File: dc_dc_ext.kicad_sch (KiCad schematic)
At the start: 30 parts, among them U10 TPS56339DDC, U11 TPS56339DDC

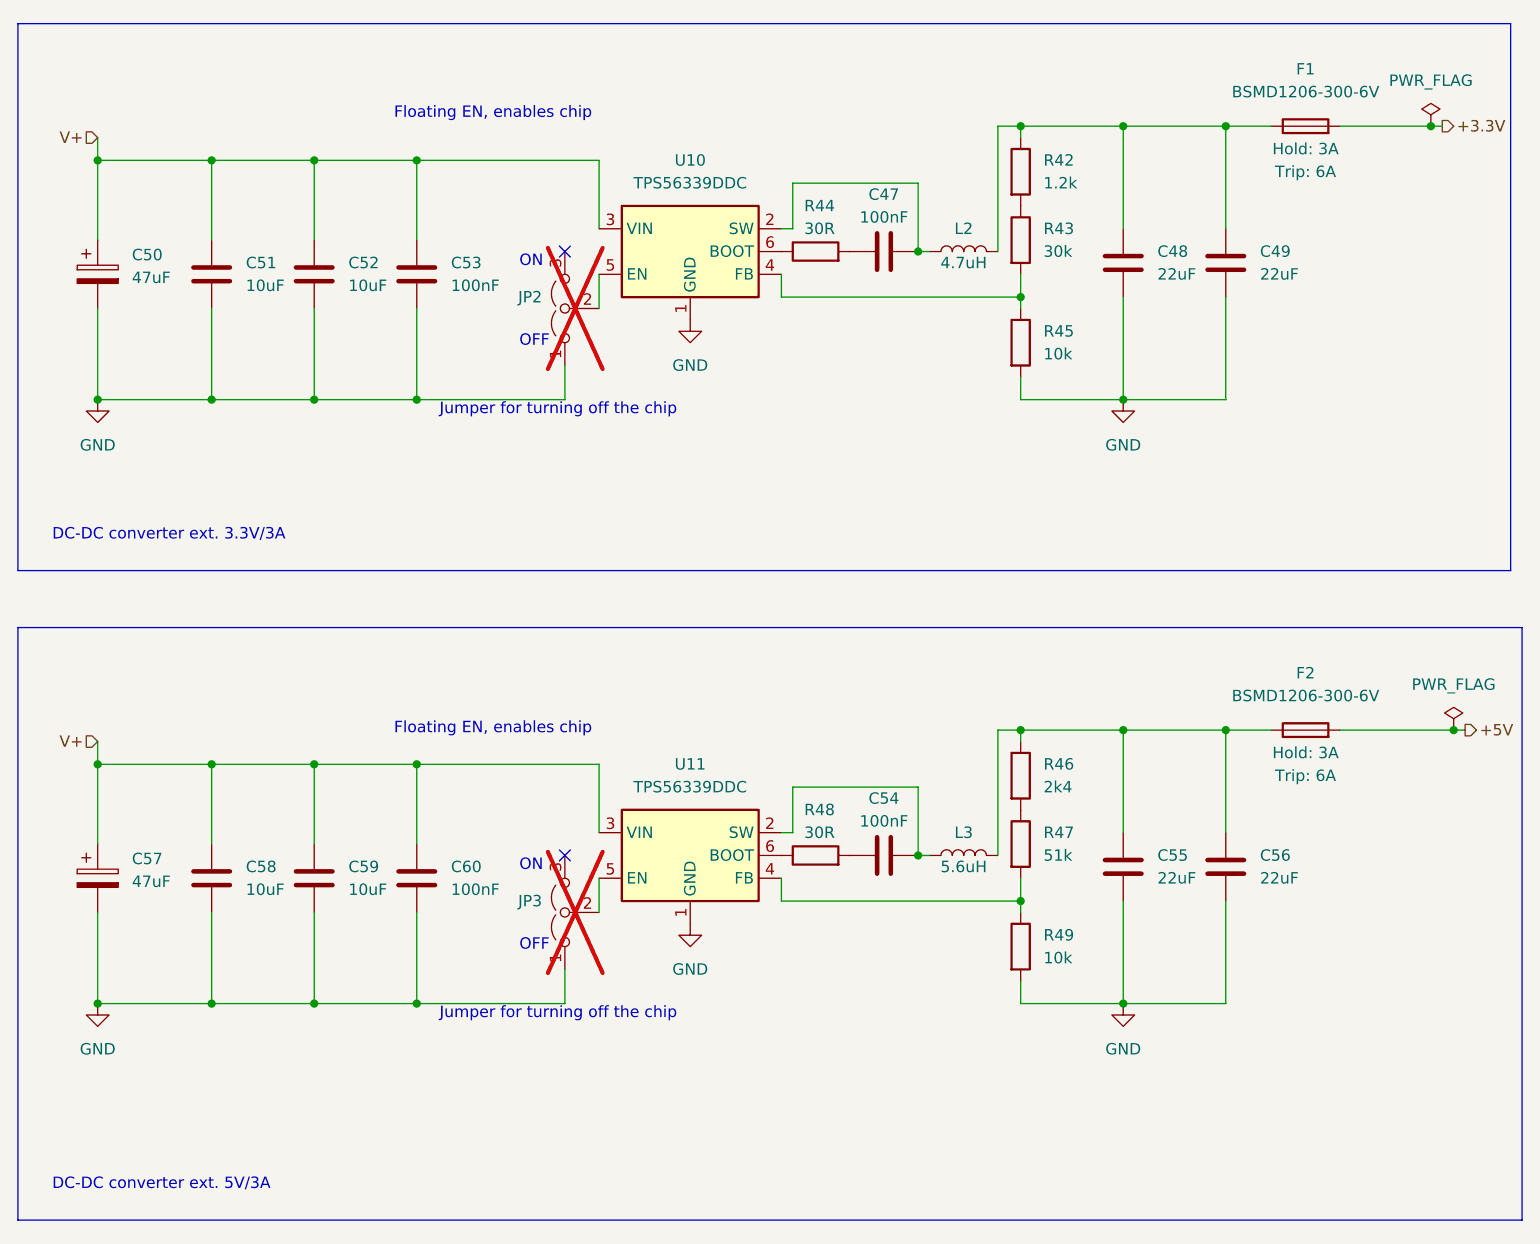
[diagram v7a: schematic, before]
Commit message: updated to kicad 9, added comparator-based power source switching
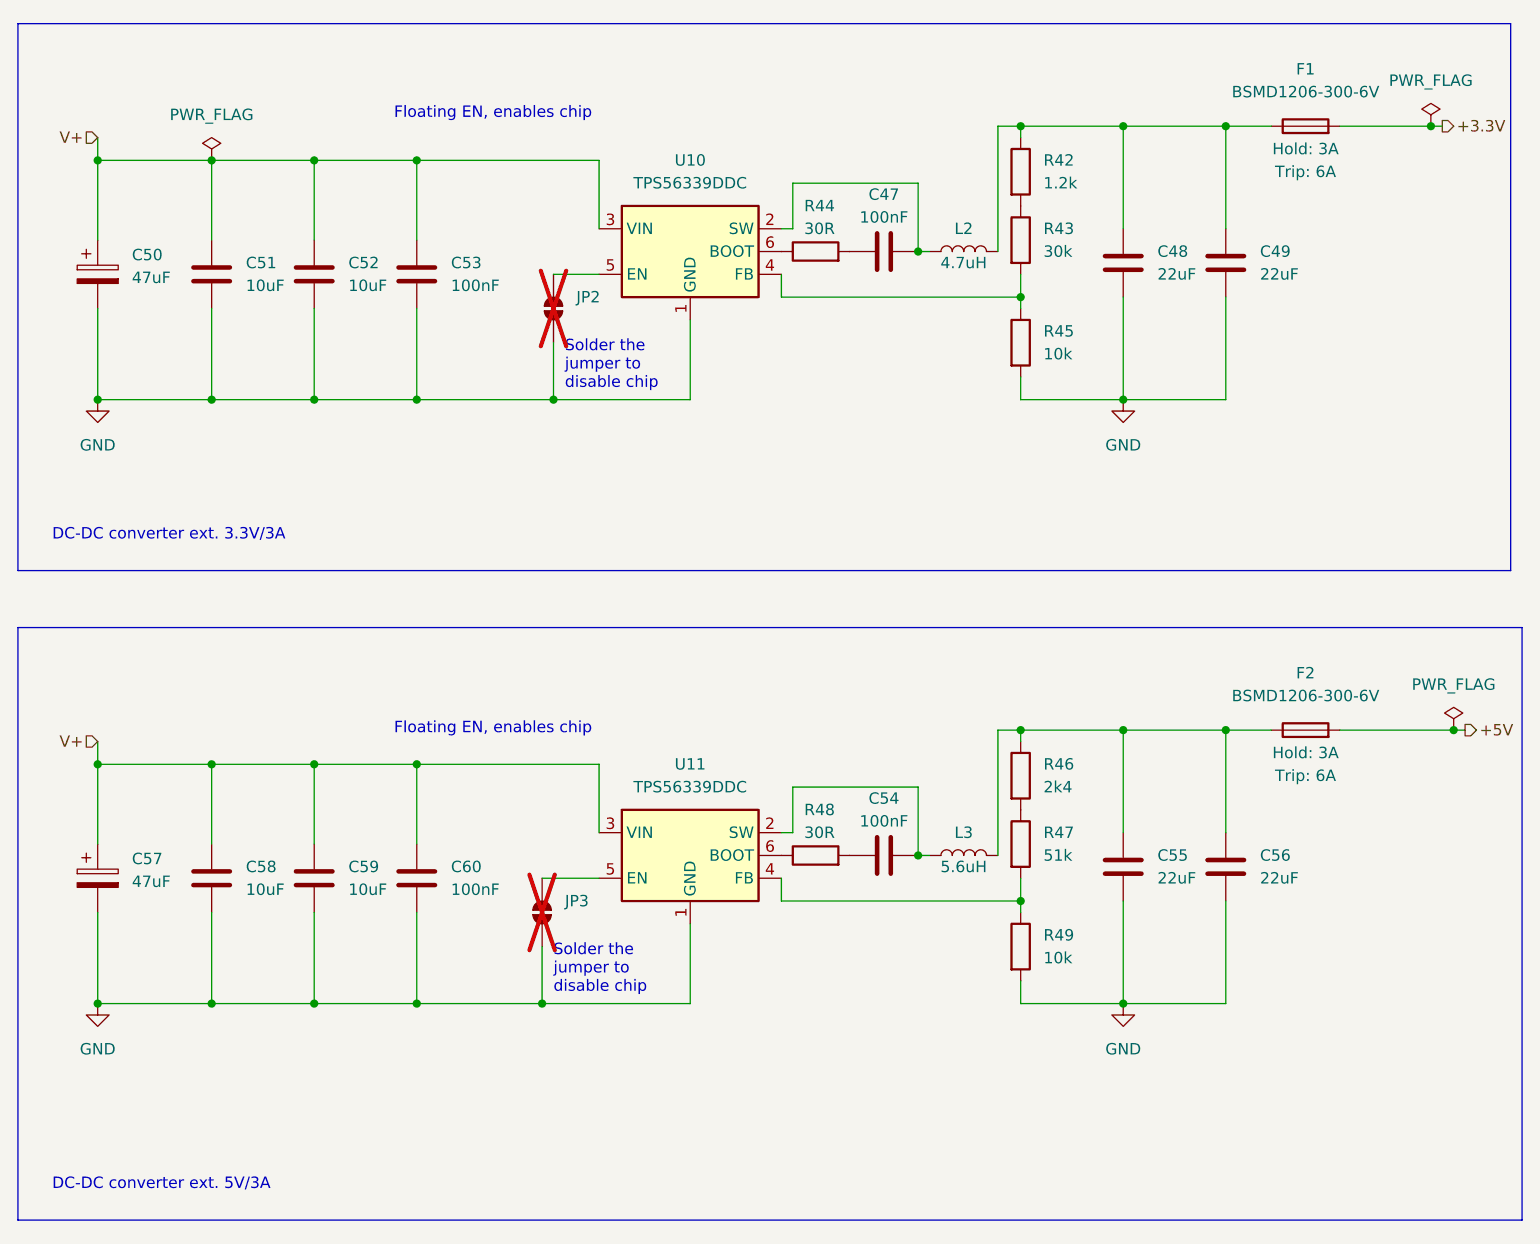
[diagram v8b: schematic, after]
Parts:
- removed JP2, JP3: (no value), Connector_PinHeader_2.54mm:PinHeader_1x03_P2.54mm_Vertical, symbol Jumper:Jumper_3_Open
- added JP2, JP3: SolderJumper_2_Open, Jumper:SolderJumper-2_P1.3mm_Open_RoundedPad1.0x1.5mm, symbol Jumper:SolderJumper_2_Open
- F1, F2: value BSMD1206-300-6V -> BSMD1206-300-6V
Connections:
- net GND: now also JP2.1 (A), JP3.1 (A)
- net at U11.5 (EN): now also JP3.2 (B)
- net at U10.5 (EN): now also JP2.2 (B)
- no-connect marks 2 -> 0
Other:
- note added: "Solder the jumper to disable chip"
- note removed: "Jumper for turning off the chip"
- note removed: "OFF"
- note removed: "ON"
